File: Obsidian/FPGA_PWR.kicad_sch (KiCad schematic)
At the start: 52 parts, among them U1 XC7A35T-CSG325

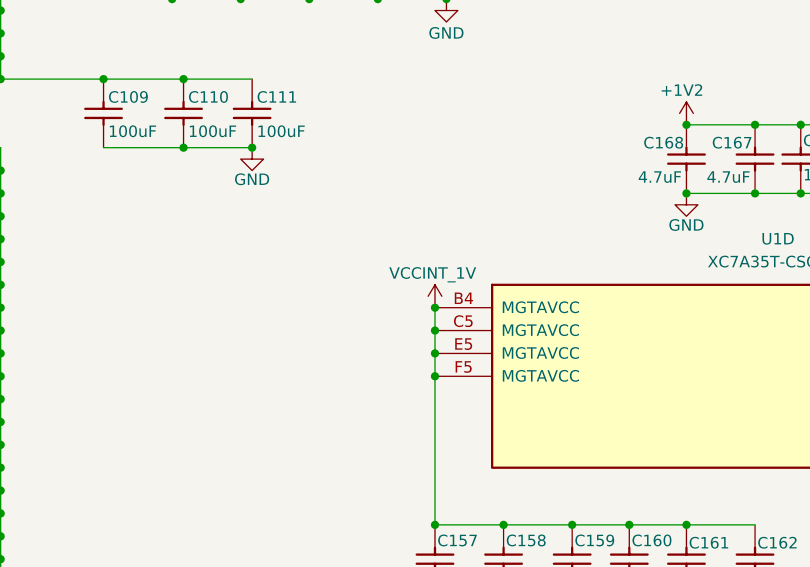
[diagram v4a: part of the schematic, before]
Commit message: adding 1V regulator for MGT transceiver
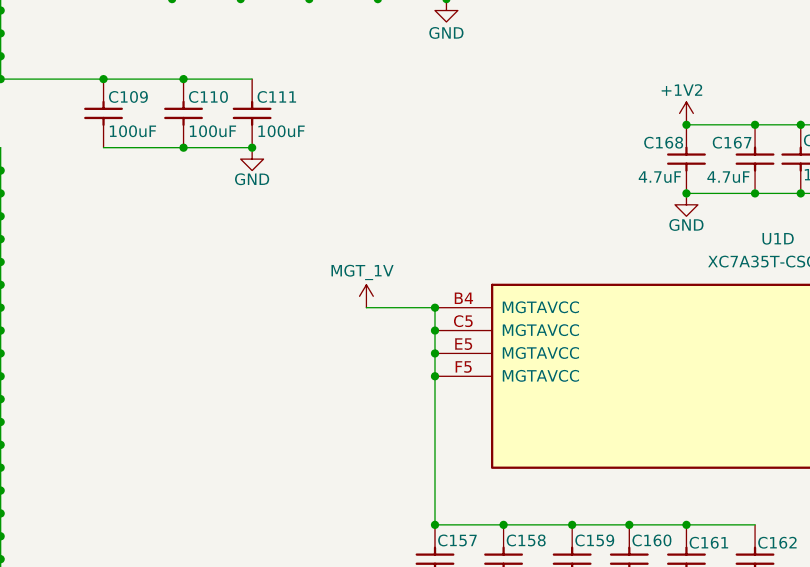
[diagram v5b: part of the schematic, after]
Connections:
- net VCCINT_1V: no longer C157.2, C158.2, C159.2, C160.2, C161.2, C162.2, U1.B4 (MGTAVCC), U1.C5 (MGTAVCC), U1.E5 (MGTAVCC), U1.F5 (MGTAVCC)
- new net MGT_1V: C157.2, C158.2, C159.2, C160.2, C161.2, C162.2, U1.B4 (MGTAVCC), U1.C5 (MGTAVCC), U1.E5 (MGTAVCC), U1.F5 (MGTAVCC)
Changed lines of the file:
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@@
+	(wire
+		(pts
+			(xy 167.64 100.33) (xy 175.26 100.33)
+		)
+		(stroke
+			(width 0)
+			(type default)
+		)
+	)
 	(wire
 		(pts
@@
 	(symbol
 		(lib_id "Library_Symbol:+1V0")
-		(at 175.26 100.33 0)
+		(at 167.64 100.33 0)
 		(unit 1)
 		(exclude_from_sim no)
@@
 		(dnp no)
 		(property "Reference" "#PWR0261"
-			(at 175.26 104.14 0)
+			(at 167.64 104.14 0)
 			(effects
 				(font
@@
 			)
 		)
-		(property "Value" "VCCINT_1V"
-			(at 175.006 96.52 0)
+		(property "Value" "MGT_1V"
+			(at 167.132 96.266 0)
 			(effects
 				(font
@@
 		)
 		(property "Footprint" ""
-			(at 175.26 100.33 0)
+			(at 167.64 100.33 0)
 			(effects
 				(font
@@
 		)
 		(property "Datasheet" ""
-			(at 175.26 100.33 0)
+			(at 167.64 100.33 0)
 			(effects
 				(font
@@
 		)
 		(property "Description" "Power symbol creates a global label with name \"+1V0\""
-			(at 175.26 100.33 0)
+			(at 167.64 100.33 0)
 			(effects
 				(font

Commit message: Cleaning symbol fields
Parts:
- C100, C101, C102, C112, C121, C97, C98, C99: Author CERN DEM JLC -> (none); Case 0201 -> (none); Comment 47nF -> (none); Component Kind Standard -> (none); Component Type Standard -> (none); ComponentHeight (none) -> (none); CreateDate 12/03/07 00:00:00 -> (none); Database Table Name Capacitors -> (none); Footprint Library Capacitors SMD -> (none); Footprint Path PcbLib\Capacitors SMD.PcbLib -> (none); Footprint Ref CAPC0603X33N -> (none); HelpURL \\cern.ch\dfs\Applications\Altium\Datasheets\CC0201_X5R_AVX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 -> (none); LatestRevisionDate 12/03/07 00:00:00 -> (none); Library Name Capacitors SMD -> (none); Library Path SchLib\Capacitors.SchLib -> (none); Library Ref Capacitor - non polarized -> (none); License CC-BY-SA 4.0 -> (none); Manufacturer GENERIC -> (none); Manufacturer Part Number CC0201_47NF_6.3V_10%_X5R -> (none); Manufacturer1 ComponentHeight 0.33mm -> (none); Manufacturer1 Example AVX -> (none); Manufacturer1 Part Number 02016D473KAT2A -> (none); Mounted Yes -> (none); PackageDescription (none) -> (none); Part Description SMD Multilayer Chip Ceramic Capacitor -> (none); Part Number CC0201_47NF_6.3V_10%_X5R -> (none); Pin Count 2 -> (none); PressFit (none) -> (none); SMD Yes -> (none); Sense No -> (none); Sense Comment (none) -> (none); Socket No -> (none); Status Not Recommended -> (none); Status Comment (none) -> (none); TC X5R -> (none); Tolerance ±10% -> (none); Voltage 6.3V -> (none)
- C103, C104, C105, C106, C107, C108, C117, C118, C156, C161, C162, C167, C168: Author CERN DEM BC -> (none); Case 0402 -> (none); Comment 4.7uF -> (none); Component Kind Standard -> (none); Component Type Standard -> (none); ComponentHeight (none) -> (none); CreateDate 09/07/20 00:00:00 -> (none); Database Table Name Capacitors -> (none); Footprint Library Capacitors SMD -> (none); Footprint Path PcbLib\Capacitors SMD.PcbLib -> (none); Footprint Ref CAPC1005X55N -> (none); HelpURL \\cern.ch\dfs\Applications\Altium\Datasheets\CC0402_X5R_YAG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 -> (none); LatestRevisionDate 09/07/20 00:00:00 -> (none); Library Name Capacitors SMD -> (none); Library Path SchLib\Capacitors.SchLib -> (none); Library Ref Capacitor - non polarized -> (none); License CC-BY-SA 4.0 -> (none); Manufacturer GENERIC -> (none); Manufacturer Part Number CC0402_4.7UF_16V_20%_X5R -> (none); Manufacturer1 ComponentHeight 0.55mm -> (none); Manufacturer1 Example YAGEO PHYCOMP -> (none); Manufacturer1 Part Number CC0402MRX5R7BB475 -> (none); Mounted Yes -> (none); PackageDescription (none) -> (none); Part Description SMD Multilayer Chip Ceramic Capacitor -> (none); Part Number CC0402_4.7UF_16V_20%_X5R -> (none); Pin Count 2 -> (none); PressFit (none) -> (none); SMD Yes -> (none); Sense No -> (none); Sense Comment (none) -> (none); Socket No -> (none); Status Preferred -> (none); Status Comment (none) -> (none); TC X5R -> (none); Tolerance ±20% -> (none); Voltage 16V -> (none)
- C109, C110, C111, C119, C122: Author CERN DEM BC -> (none); Case 0805 -> (none); Comment 100uF -> (none); Component Kind Standard -> (none); Component Type Standard -> (none); ComponentHeight (none) -> (none); CreateDate 01/10/20 00:00:00 -> (none); Database Table Name Capacitors -> (none); Footprint Library Capacitors SMD -> (none); Footprint Path PcbLib\Capacitors SMD.PcbLib -> (none); Footprint Ref CAPC2012X145N -> (none); HelpURL \\cern.ch\dfs\Applications\Altium\Datasheets\CC0805_MURATA_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 -> (none); LatestRevisionDate 01/10/20 00:00:00 -> (none); Library Name Capacitors SMD -> (none); Library Path SchLib\Capacitors.SchLib -> (none); Library Ref Capacitor - non polarized -> (none); License CC-BY-SA 4.0 -> (none); Manufacturer GENERIC -> (none); Manufacturer Part Number CC0805_100UF_6.3V_20%_X5R -> (none); Manufacturer1 ComponentHeight 1.45mm -> (none); Manufacturer1 Example MURATA -> (none); Manufacturer1 Part Number GRM21BR60J107ME15 -> (none); Mounted Yes -> (none); PackageDescription (none) -> (none); Part Description SMD Multilayer Chip Ceramic Capacitor -> (none); Part Number CC0805_100UF_6.3V_20%_X5R -> (none); Pin Count 2 -> (none); PressFit (none) -> (none); SMD Yes -> (none); Sense No -> (none); Sense Comment (none) -> (none); Socket No -> (none); Status Preferred -> (none); Status Comment (none) -> (none); TC X5R -> (none); Tolerance ±20% -> (none); Voltage 6.3V -> (none)
- C113, C114, C115, C116, C120, C155, C89, C90, C91, C92, C93, C94, C95, C96: Author CERN DEM JLC -> (none); Case 0201 -> (none); Comment 470nF -> (none); Component Kind Standard -> (none); Component Type Standard -> (none); ComponentHeight (none) -> (none); CreateDate 05/27/10 00:00:00 -> (none); Database Table Name Capacitors -> (none); Footprint Library Capacitors SMD -> (none); Footprint Path PcbLib\Capacitors SMD.PcbLib -> (none); Footprint Ref CAPC0603X33N -> (none); HelpURL \\cern.ch\dfs\Applications\Altium\Datasheets\CC0201_X5R_TAI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 -> (none); LatestRevisionDate 05/27/10 00:00:00 -> (none); Library Name Capacitors SMD -> (none); Library Path SchLib\Capacitors.SchLib -> (none); Library Ref Capacitor - non polarized -> (none); License CC-BY-SA 4.0 -> (none); Manufacturer GENERIC -> (none); Manufacturer Part Number CC0201_470NF_4V_20%_X5R -> (none); Manufacturer1 ComponentHeight 0.33mm -> (none); Manufacturer1 Example TAIYO YUDEN -> (none); Manufacturer1 Part Number AMK063BJ474MP-F -> (none); Mounted Yes -> (none); PackageDescription (none) -> (none); Part Description SMD Multilayer Chip Ceramic Capacitor -> (none); Part Number CC0201_470NF_4V_20%_X5R -> (none); Pin Count 2 -> (none); PressFit (none) -> (none); SMD Yes -> (none); Sense No -> (none); Sense Comment (none) -> (none); Socket No -> (none); Status Not Recommended -> (none); Status Comment (none) -> (none); TC X5R -> (none); Tolerance ±20% -> (none); Voltage 4V -> (none)
- C157, C158, C159, C160, C163, C164, C165, C166, C169: Author CERN DEM JLC -> (none); Case 0201 -> (none); Comment 100nF -> (none); Component Kind Standard -> (none); Component Type Standard -> (none); ComponentHeight (none) -> (none); CreateDate 12/03/07 00:00:00 -> (none); Database Table Name Capacitors -> (none); Footprint Library Capacitors SMD -> (none); Footprint Path PcbLib\Capacitors SMD.PcbLib -> (none); Footprint Ref CAPC0603X33N -> (none); HelpURL \\cern.ch\dfs\Applications\Altium\Datasheets\CC0201_X5R_AVX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 -> (none); LatestRevisionDate 12/03/07 00:00:00 -> (none); Library Name Capacitors SMD -> (none); Library Path SchLib\Capacitors.SchLib -> (none); Library Ref Capacitor - non polarized -> (none); License CC-BY-SA 4.0 -> (none); Manufacturer GENERIC -> (none); Manufacturer Part Number CC0201_100NF_6.3V_10%_X5R -> (none); Manufacturer1 ComponentHeight 0.33mm -> (none); Manufacturer1 Example AVX -> (none); Manufacturer1 Part Number 02016D104KAT2A -> (none); Mounted Yes -> (none); PackageDescription (none) -> (none); Part Description SMD Multilayer Chip Ceramic Capacitor -> (none); Part Number CC0201_100NF_6.3V_10%_X5R -> (none); Pin Count 2 -> (none); PressFit (none) -> (none); SMD Yes -> (none); Sense No -> (none); Sense Comment (none) -> (none); Socket No -> (none); Status Not Recommended -> (none); Status Comment (none) -> (none); TC X5R -> (none); Tolerance ±10% -> (none); Voltage 6.3V -> (none)
- L16: Author CERN DEM JLC -> (none); Case 0402 -> (none); Comment 220R@100MHz -> (none); Component Kind Standard -> (none); Component Type Standard -> (none); ComponentHeight 0.55mm -> (none); CreateDate 06/23/09 00:00:00 -> (none); Database Table Name Inductors & Transformers -> (none); Footprint Library Inductors SMD -> (none); Footprint Path PcbLib\Inductors SMD.PcbLib -> (none); Footprint Ref INDC1005X55N -> (none); HelpURL \\cern.ch\dfs\Applications\Altium\Datasheets\IND0402_MURATA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 -> (none); LatestRevisionDate 10/25/18 00:00:00 -> (none); Library Name Inductors SMD -> (none); Library Path SchLib\Inductors & Transformers.SchLib -> (none); Library Ref Ferrite Bead -> (none); License CC-BY-SA 4.0 -> (none); Manufacturer MURATA -> (none); Manufacturer Part Number BLM15HB221SN1 -> (none); Mounted Yes -> (none); PackageDescription (none) -> (none); Part Description SMD EMIFIL Suppression Chip Ferrite Bead -> (none); Part Number IND0402_MURATA_BLM15HB221SN1 -> (none); Pin Count 2 -> (none); Power 250mA -> (none); Resistance 1R -> (none); SMD Yes -> (none); Sense No -> (none); Sense Comment (none) -> (none); Socket No -> (none); Status (none) -> (none); Status Comment (none) -> (none); Tolerance ±25% -> (none)
- R114: Case 0402 -> (none); Comment =Value -> (none); Component Kind Standard -> (none); Component Type Standard -> (none); ComponentHeight (none) -> (none); CreateDate 12/12/13 00:00:00 -> (none); Database Table Name Resistors -> (none); Footprint Library Resistors SMD -> (none); Footprint Path PcbLib\Resistors SMD.PcbLib -> (none); Footprint Ref RESC1005X40N -> (none); HelpURL \\cern.ch\dfs\Applications\Altium\Datasheets\R0402_Phycomp_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 -> (none); LatestRevisionDate 03/03/15 00:00:00 -> (none); Library Name Resistors SMD -> (none); Library Path SchLib\Resistors.SchLib -> (none); Library Ref Resistor - 1% -> (none); License This work is licensed under the Creative Commons CC-BY-SA 4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 -> (none); Manufacturer GENERIC -> (none); Manufacturer Part Number R0402_100R_1%_0.1W_100PPM -> (none); Manufacturer1 ComponentHeight 0.4mm -> (none); Manufacturer1 Example PANASONIC -> (none); Manufacturer1 Part Number ERJ2RKF1000X -> (none); Mounted Yes -> (none); PackageDescription (none) -> (none); Part Description General Purpose Thick Film Chip Resistor -> (none); Part Number R0402_100R_1%_0.1W_100PPM -> (none); Pin Count 2 -> (none); Power 0.1W -> (none); PressFit No -> (none); SMD Yes -> (none); Sense No -> (none); Sense Comment (none) -> (none); Socket No -> (none); Status Not Recommended -> (none); Status Comment (none) -> (none); TC ±100ppm/°C -> (none); Tolerance ±1% -> (none); Voltage 50V -> (none)
